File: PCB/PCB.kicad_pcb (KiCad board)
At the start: 2 copper layers, 16 parts, among them J1 USB_B_Micro, Q1 PJA3428, Q2 PJA3428, Q3 AO3401A, Q4 BD441, U2 CP2102N-Axx-xQFN24, U4 LM2578

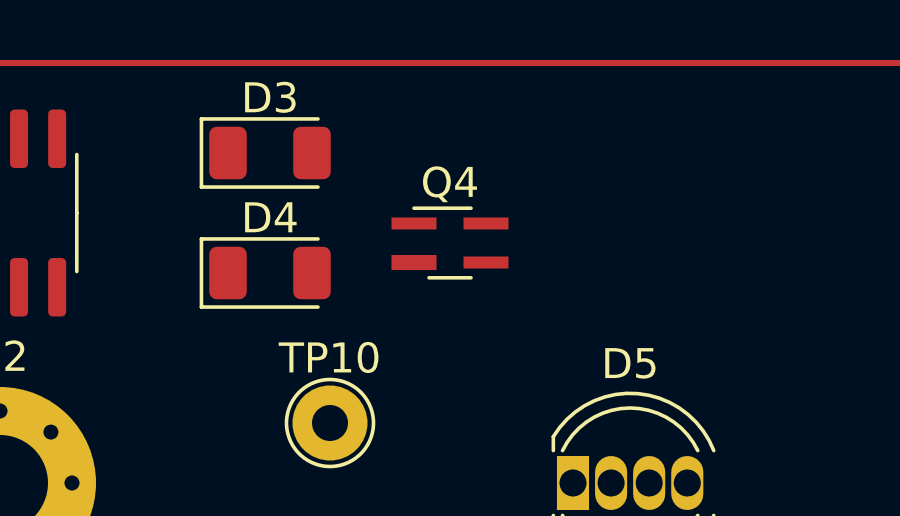
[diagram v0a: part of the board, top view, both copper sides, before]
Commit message: pcb update (transistors)
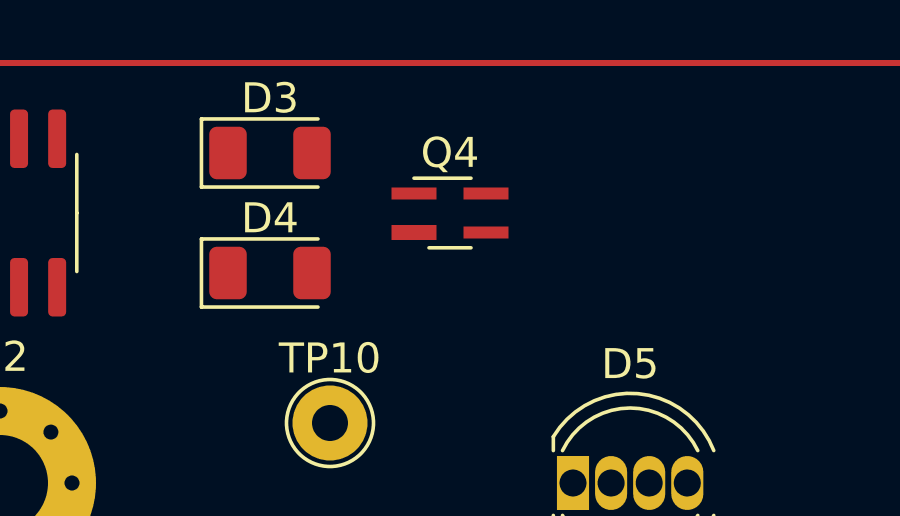
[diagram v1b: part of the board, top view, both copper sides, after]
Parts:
- Q4: value BD441 -> BC546
- moved Q4 1.00 mm to (149.0, 96.0)
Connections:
- Q4 pad 1: GND -> Net-(D4-Pad2)
- Q4 pad 2: Net-(D4-Pad2) -> Net-(R14-Pad1)
- Q4 pad 3: Net-(Q4-Pad3) -> GND

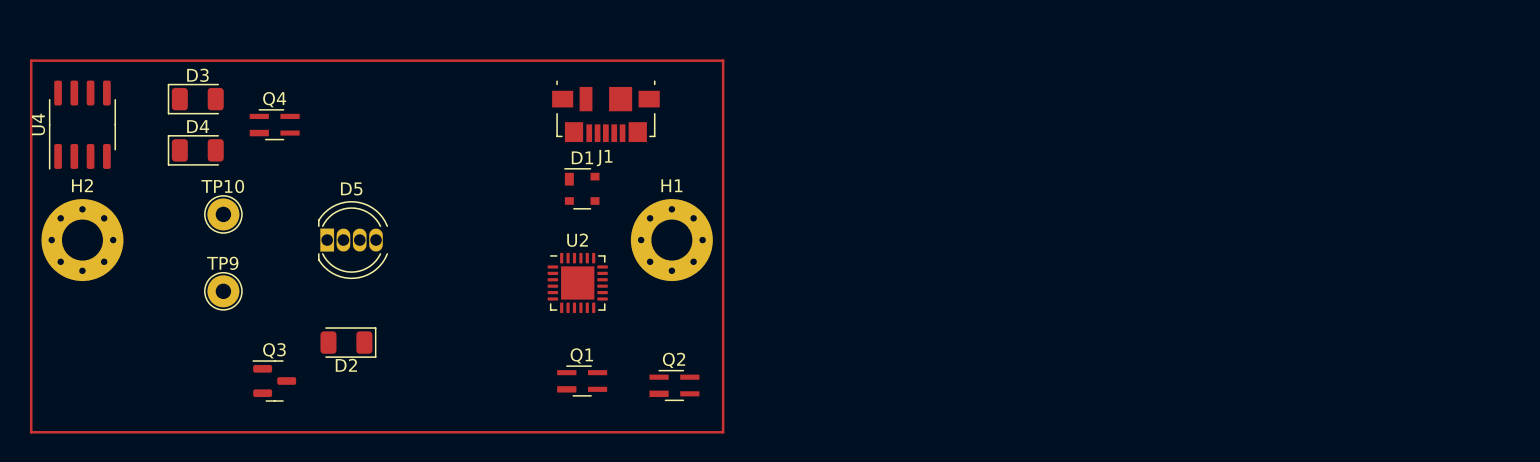
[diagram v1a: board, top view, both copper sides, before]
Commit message: edge cut improvement and general placements for mechanical design
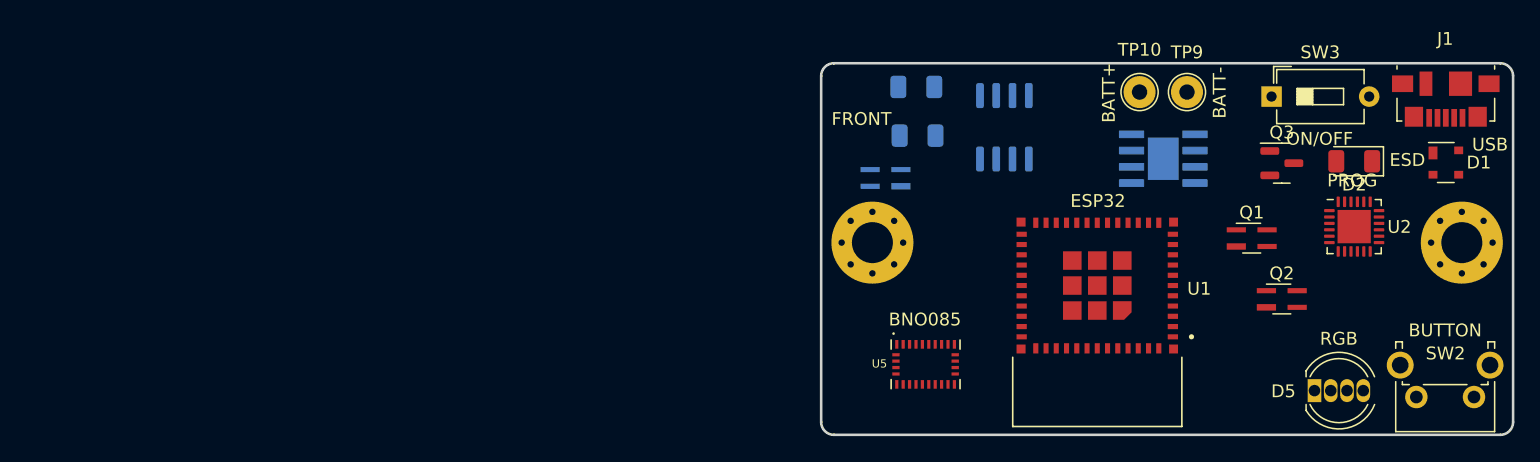
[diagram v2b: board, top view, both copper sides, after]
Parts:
- added SW2: SW_Push, Button_Switch_THT:SW_Tactile_SPST_Angled_PTS645Vx58-2LFS, F.Cu at (242.6, 117.2)
- added SW3: ON/OFF, Button_Switch_THT:SW_DIP_SPSTx01_Slide_6.7x4.1mm_W7.62mm_P2.54mm_LowProfile, F.Cu at (226.8, 93.8)
- added U1: ESP32-PICO-MINI-02, ESP32-PICO-MINI-02:MODULE_ESP32-PICO-MINI-02, F.Cu at (213.2, 108.5)
- added U3: TP4056, TP4056:SOP127P600X175-9N, B.Cu at (218.3, 98.7)
- added U5: BNO080, BNO080:IC_BNO080, F.Cu at (199.8, 114.7)
- D3, D4, Q4, U4: moved to B.Cu
- moved Q3 80.4 mm to (227.6, 99.0)
- moved D2 79.9 mm to (233.2, 98.8)
- moved D5 77.9 mm to (230.2, 116.8)
- moved TP9 76.8 mm to (220.2, 93.5)
- moved TP10 72.1 mm to (216.5, 93.5)
- moved U4 72.0 mm to (205.9, 96.2)
- moved D1 67.4 mm to (240.4, 99.0)
- moved J1 65.6 mm to (240.4, 94.0)
- moved H1 61.7 mm to (241.7, 105.2)
- moved H2 61.7 mm to (195.7, 105.2)
- moved U2 60.8 mm to (233.2, 104.0)
- moved D4 56.2 mm to (199.2, 96.8), turned to 180 degrees
- moved D3 56.1 mm to (199.1, 93.0), turned to 180 degrees
- moved Q1 53.4 mm to (225.2, 104.8)
- moved Q2 47.9 mm to (227.6, 109.6)
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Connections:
- U2 pad 18: FTDI_CTS -> (no net)
- U2 pad 19: FTDI_RTS -> (no net)
- U2 pad 20: FTDI_RX -> (no net)
- U2 pad 21: FTDI_TX -> (no net)
- U2 pad 23: FTDI_DTR -> (no net)
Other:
- board outline added: 54 x 29 mm
- board text added: "BACK"
- board text added: "BATT+"
- board text added: "BATT-"
- board text added: "BNO085"
- board text added: "BUTTON"
- board text added: "ESD"
- board text added: "ESP32"
- board text added: "FRONT"
- board text added: "LM2578"
- board text added: "ON/OFF"
- board text added: "PROG"
- board text added: "RGB"
- board text added: "TP4056"
- board text added: "USB"

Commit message: huuuuge progress
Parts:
- added C1: 10uF, Capacitor_SMD:C_0603_1608Metric, F.Cu at (240.9, 66.1)
- added C10: 100nF, Capacitor_SMD:C_0603_1608Metric, F.Cu at (236.3, 103.9)
- added C11: 100nF, Capacitor_SMD:C_0603_1608Metric, F.Cu at (198.7, 118.4)
- added C15: 22pf, Capacitor_SMD:C_0603_1608Metric, F.Cu at (201.5, 109.4)
- added C16: 22pf, Capacitor_SMD:C_0603_1608Metric, F.Cu at (194.2, 109.4)
- added C18: 12pf, Capacitor_SMD:C_0603_1608Metric, F.Cu at (269.6, 43.3)
- added C19: 12pf, Capacitor_SMD:C_0603_1608Metric, F.Cu at (255.7, 57.8)
- added C2: 1uF, Capacitor_SMD:C_0603_1608Metric, F.Cu at (251.2, 61.4)
- added C20: 1uF, Capacitor_SMD:C_0603_1608Metric, F.Cu at (251.7, 57.8)
- added C21: 10uF, Capacitor_SMD:C_1206_3216Metric, B.Cu at (236.9, 98.5)
- added C22: 10uF, Capacitor_SMD:C_1206_3216Metric, B.Cu at (231.9, 92.6)
- added C23: 100nF, Capacitor_SMD:C_0603_1608Metric, F.Cu at (193.4, 113.4)
- added C24: 100nF, Capacitor_SMD:C_0603_1608Metric, F.Cu at (193.4, 111.8)
- added C3: 10uF, Capacitor_SMD:C_0603_1608Metric, F.Cu at (265.6, 45.8)
- added C4: 1uF, Capacitor_SMD:C_0603_1608Metric, F.Cu at (248.9, 64.0)
- added C5: 100nF, Capacitor_SMD:C_0603_1608Metric, F.Cu at (237.8, 72.5)
- added C6: 100nF, Capacitor_SMD:C_0603_1608Metric, F.Cu at (256.9, 50.9)
- added C7: 10uF, Capacitor_SMD:C_1206_3216Metric, F.Cu at (224.5, 96.2)
- added C8: 100nF, Capacitor_SMD:C_0603_1608Metric, F.Cu at (233.3, 102.2)
- added C9: 1uF, Capacitor_SMD:C_0603_1608Metric, F.Cu at (237.9, 103.9)
- added D6: LED_RGB, LED_THT:LED_D5.0mm-4_RGB, F.Cu at (234.6, 116.8)
- added D7: Red, LED_SMD:LED_0805_2012Metric_Pad1.15x1.40mm_HandSolder, B.Cu at (231.6, 95.0)
- added D8: Green, LED_SMD:LED_0805_2012Metric_Pad1.15x1.40mm_HandSolder, B.Cu at (231.6, 97.1)
- added F1: 500mA, 0ZCJ0050FF2G:RESC3216X125N, F.Cu at (229.3, 97.2)
- added R1: 10k, Resistor_SMD:R_0603_1608Metric, F.Cu at (232.3, 76.0)
- added R11: 10k, Resistor_SMD:R_0603_1608Metric, F.Cu at (200.3, 118.4)
- added R15: 3.3k, Resistor_SMD:R_0603_1608Metric, F.Cu at (204.7, 106.9)
- added R16: 3.3k, Resistor_SMD:R_0603_1608Metric, F.Cu at (203.1, 106.9)
- added R17: 1k, Resistor_SMD:R_0603_1608Metric, F.Cu at (244.9, 64.0)
- added R18: 10k, Resistor_SMD:R_0603_1608Metric, F.Cu at (251.7, 55.3)
- added R19: 470, Resistor_SMD:R_0603_1608Metric, F.Cu at (225.3, 94.2)
- added R2: 10k, Resistor_SMD:R_0603_1608Metric, F.Cu at (248.9, 66.5)
- added R20: 2k, Resistor_SMD:R_0603_1608Metric, B.Cu at (243.9, 93.7)
- added R21: 10k, Resistor_SMD:R_0603_1608Metric, F.Cu at (241.8, 69.0)
- added R22: 470, Resistor_SMD:R_0603_1608Metric, B.Cu at (227.9, 95.2)
- added R23: 470, Resistor_SMD:R_0603_1608Metric, B.Cu at (227.9, 96.9)
- added R24: 3.3k, Resistor_SMD:R_0603_1608Metric, F.Cu at (265.4, 48.3)
- added R25: 3.3k, Resistor_SMD:R_0603_1608Metric, F.Cu at (236.3, 75.0)
- added R3: 10k, Resistor_SMD:R_0603_1608Metric, F.Cu at (228.3, 76.0)
- added R4: 10k, Resistor_SMD:R_0603_1608Metric, F.Cu at (244.9, 66.5)
- added R5: 22k, Resistor_SMD:R_0603_1608Metric, F.Cu at (237.9, 100.8)
- added R6: 47k, Resistor_SMD:R_0603_1608Metric, F.Cu at (236.3, 100.8)
- added R7: 10k, Resistor_SMD:R_0603_1608Metric, F.Cu at (204.1, 113.7)
- added R8: 10k, Resistor_SMD:R_0603_1608Metric, F.Cu at (193.4, 115.0)
- added SW1: SW_Push, Button_Switch_SMD:SW_SPST_CK_KXT3, F.Cu at (218.4, 67.9)
- added SW4: ON/OFF, footprints:CUS-12TB, F.Cu at (231.4, 92.7)
- added TP11: ~{RESET}_TP, TestPoint:TestPoint_Pad_D1.0mm, F.Cu at (243.8, 74.8)
- added TP12: GPIO0_TP, TestPoint:TestPoint_Pad_D1.0mm, F.Cu at (252.4, 67.3)
- added TP13: SDA_TP, TestPoint:TestPoint_Pad_D1.0mm, F.Cu at (259.2, 59.1)
- added TP14: SCL_TP, TestPoint:TestPoint_Pad_D1.0mm, F.Cu at (249.4, 69.2)
- added TP15: INT_TP, TestPoint:TestPoint_Pad_D1.0mm, F.Cu at (202.3, 117.8)
- added TP3: InputVoltage_TP, TestPoint:TestPoint_Pad_D1.0mm, F.Cu at (268.9, 48.6)
- added TP4: TX_TP, TestPoint:TestPoint_Pad_D1.0mm, F.Cu at (273.1, 46.6)
- added TP5: RX_TP, TestPoint:TestPoint_Pad_D1.0mm, F.Cu at (252.4, 64.2)
- added TP6: RTS_TP, TestPoint:TestPoint_Pad_D1.0mm, F.Cu at (259.2, 56.1)
- added TP7: CTS_TP, TestPoint:TestPoint_Pad_D1.0mm, F.Cu at (245.4, 71.8)
- added TP8: DTR_TP, TestPoint:TestPoint_Pad_D1.0mm, F.Cu at (262.3, 56.1)
- added Y1: 32.768 kHz, Crystal:Crystal_SMD_EuroQuartz_EQ161-2Pin_3.2x1.5mm, F.Cu at (197.9, 109.8)
- added Y2: 32.768 kHz, Crystal:Crystal_SMD_EuroQuartz_EQ161-2Pin_3.2x1.5mm, F.Cu at (235.8, 67.0)
- D5: value LED_RGBA -> PowerLed; footprint LED_THT:LED_D5.0mm-4_RGB -> LED_SMD:LED_0805_2012Metric_Pad1.15x1.40mm_HandSolder
- H1, H2: footprint MountingHole:MountingHole_3.2mm_M3_Pad_Via -> MountingHole:MountingHole_2.2mm_M2_Pad_Via
- SW2: footprint Button_Switch_THT:SW_Tactile_SPST_Angled_PTS645Vx58-2LFS -> Button_Switch_SMD:SW_SPST_CK_KXT3
- SW3: value ON/OFF -> SW_Push; footprint Button_Switch_THT:SW_DIP_SPSTx01_Slide_6.7x4.1mm_W7.62mm_P2.54mm_LowProfile -> Button_Switch_SMD:SW_SPST_CK_KXT3
- U1: footprint ESP32-PICO-MINI-02:MODULE_ESP32-PICO-MINI-02 -> ESP32:MODULE_ESP32-PICO-MINI-02
- U4: moved to F.Cu
- moved SW2 59.6 mm to (218.4, 62.7), turned to 0 degrees
- moved SW3 49.7 mm to (233.9, 44.6)
- moved U4 25.2 mm to (217.2, 73.7), turned to 0 degrees
- moved D5 24.9 mm to (224.9, 92.4), turned to 180 degrees
- moved U3 20.5 mm to (238.3, 94.3)
- moved TP10 15.1 mm to (230.0, 100.2)
- moved TP9 9.20 mm to (226.4, 100.2)
- moved Q3 6.08 mm to (233.6, 98.0), turned to -90 degrees
- moved D2 4.73 mm to (237.9, 98.0), turned to 0 degrees
- moved Q2 4.32 mm to (223.4, 110.6), turned to 180 degrees
- moved Q1 3.29 mm to (223.3, 107.5)
- moved D1 3.26 mm to (243.7, 98.7), turned to -90 degrees
- moved U2 2.74 mm to (232.1, 106.5), turned to 180 degrees
- moved H1 1.25 mm to (242.8, 105.7)
- moved H2 1.25 mm to (194.5, 105.7)
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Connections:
- D1 pad 2: USB_D+ -> USB_D-
- D1 pad 3: USB_D- -> USB_D+
- D5 pad 1: unconnected-(D5-Pad1) -> GND
- D5 pad 2: unconnected-(D5-Pad2) -> Net-(D5-Pad2)
- SW2 pad 1: (no net) -> Net-(R17-Pad1)
- SW2 pad 2: (no net) -> +3V3
- SW3 pad 1: (no net) -> GND
- SW3 pad 2: (no net) -> SESSION_BUTTON
- TP10 pad 1: unconnected-(TP10-Pad1) -> +BATT
- TP9 pad 1: unconnected-(TP9-Pad1) -> GND
- U1 pad 10: (no net) -> unconnected-(U1-Pad10)
- U1 pad 12: (no net) -> XTAL_0
- U1 pad 13: (no net) -> XTAL_1
- U1 pad 15: (no net) -> unconnected-(U1-Pad15)
- U1 pad 16: (no net) -> unconnected-(U1-Pad16)
- U1 pad 17: (no net) -> ~{BNO_RST}
- U1 pad 18: (no net) -> RGB_BLUE
- U1 pad 19: (no net) -> RGB_RED
- U1 pad 20: (no net) -> RGB_GREEN
- U1 pad 21: (no net) -> unconnected-(U1-Pad21)
- U1 pad 22: (no net) -> Net-(R3-Pad2)
- U1 pad 24: (no net) -> BNO_INTERRUPT
- U1 pad 25: (no net) -> unconnected-(U1-Pad25)
- U1 pad 26: (no net) -> I2C_SCL
- U1 pad 27: (no net) -> unconnected-(U1-Pad27)
- U1 pad 28: (no net) -> unconnected-(U1-Pad28)
- U1 pad 29: (no net) -> unconnected-(U1-Pad29)
- U1 pad 30: (no net) -> FTDI_TX
- U1 pad 31: (no net) -> FTDI_RX
- U1 pad 32: (no net) -> unconnected-(U1-Pad32)
- U1 pad 33: (no net) -> unconnected-(U1-Pad33)
- U1 pad 34: (no net) -> I2C_SDA
- U1 pad 35: (no net) -> unconnected-(U1-Pad35)
- U1 pad 4: (no net) -> unconnected-(U1-Pad4)
- U1 pad 5: (no net) -> unconnected-(U1-Pad5)
- U1 pad 6: (no net) -> unconnected-(U1-Pad6)
- U1 pad 7: (no net) -> unconnected-(U1-Pad7)
- U1 pad 9: (no net) -> BATT_READ
- U2 pad 18: (no net) -> FTDI_CTS
- U2 pad 19: (no net) -> FTDI_RTS
- U2 pad 20: (no net) -> FTDI_RX
- U2 pad 21: (no net) -> FTDI_TX
- U2 pad 23: (no net) -> FTDI_DTR
- U2 pad 9: ~{RESET} -> +3V3
- U3 pad 1: (no net) -> GND
- U3 pad 2: (no net) -> Net-(R20-Pad2)
- U3 pad 3: (no net) -> GND
- U3 pad 4: (no net) -> +5V
- U3 pad 5: (no net) -> +BATT
- U3 pad 6: (no net) -> ~{STDBY}
- U3 pad 7: (no net) -> ~{CHRG}
- U3 pad 8: (no net) -> +5V
- U3 pad 9: (no net) -> unconnected-(U3-Pad9)
- U5 pad 11: (no net) -> ~{BNO_RST}
- U5 pad 14: (no net) -> BNO_INTERRUPT
- U5 pad 15: (no net) -> Net-(R15-Pad2)
- U5 pad 16: (no net) -> Net-(R16-Pad2)
- U5 pad 18: (no net) -> Net-(R7-Pad2)
- U5 pad 19: (no net) -> I2C_SCL
- U5 pad 20: (no net) -> I2C_SDA
- U5 pad 26: (no net) -> Net-(C15-Pad1)
- U5 pad 27: (no net) -> Net-(C16-Pad1)
- U5 pad 28: (no net) -> +3.3V
- U5 pad 3: (no net) -> +3.3V
- U5 pad 4: (no net) -> Net-(R8-Pad2)
- U5 pad 9: (no net) -> Net-(C11-Pad1)
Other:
- board text removed: "BACK"
- board text removed: "BATT+"
- board text removed: "BATT-"
- board text removed: "BNO085"
- board text removed: "BUTTON"
- board text removed: "ESD"
- board text removed: "ESP32"
- board text removed: "FRONT"
- board text removed: "LM2578"
- board text removed: "ON/OFF"
- board text removed: "PROG"
- board text removed: "RGB"
- board text removed: "TP4056"
- board text removed: "USB"

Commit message: bno
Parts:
- D3, D4, Q4: moved to F.Cu
- TP15, TP7: moved to B.Cu
- moved R24 87.3 mm to (204.9, 111.3), turned to -90 degrees
- moved C3 82.2 mm to (221.6, 115.2), turned to 90 degrees
- moved TP13 78.4 mm to (204.9, 115.7)
- moved C18 76.7 mm to (216.3, 98.5), turned to 90 degrees
- moved TP4 75.7 mm to (234.5, 111.7)
- moved SW3 73.3 mm to (242.4, 117.4)
- moved C6 70.0 mm to (223.1, 112.1), turned to -90 degrees
- moved TP3 65.3 mm to (222.7, 94.8)
- moved TP6 62.6 mm to (230.2, 111.5)
- moved TP8 61.3 mm to (236.6, 111.7)
- moved TP14 59.0 mm to (203.0, 105.7)
- moved C19 54.9 mm to (218.9, 98.5), turned to 90 degrees
- moved C4 53.9 mm to (224.7, 112.1), turned to -90 degrees
- moved C1 52.2 mm to (223.1, 115.2), turned to 90 degrees
- moved TP5 51.4 mm to (232.4, 111.5)
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
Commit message: more placements
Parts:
- added R26: 20k, Resistor_SMD:R_0603_1608Metric, F.Cu at (251.6, 92.9)
- added R27: 27k, Resistor_SMD:R_0603_1608Metric, F.Cu at (255.6, 92.9)
- SW3: footprint Button_Switch_SMD:SW_SPST_CK_KXT3 -> Button_Switch_THT:SW_Tactile_SPST_Angled_PTS645Vx58-2LFS
- moved D6 5.49 mm to (229.2, 116.2)
- moved R21 3.17 mm to (244.3, 111.3)
- moved SW3 0.18 mm to (242.6, 117.4), turned to 180 degrees
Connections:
- SW3 pad 1: GND -> SESSION_BUTTON
- SW3 pad 2: SESSION_BUTTON -> GND
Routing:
- added copper zone on In1.Cu, net +3.3V
- added copper zone on In2.Cu, net GND
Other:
- copper layers 2 -> 4

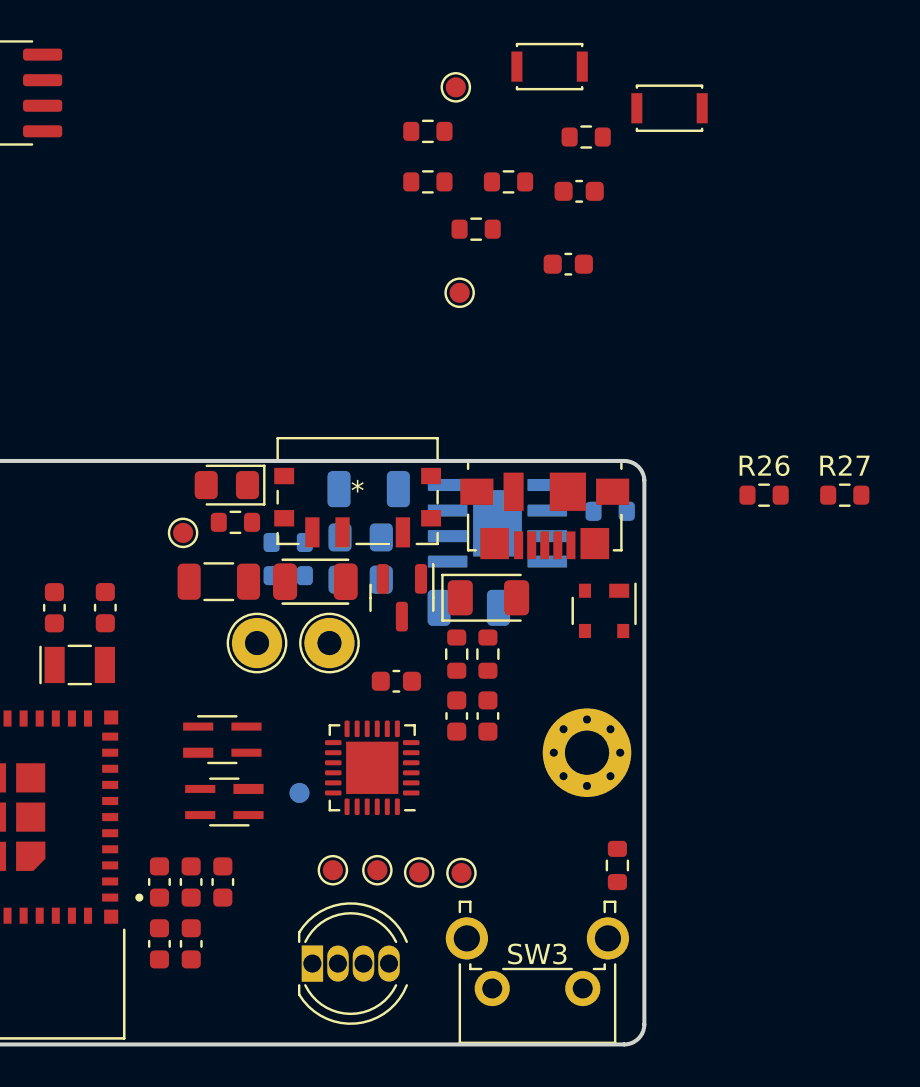
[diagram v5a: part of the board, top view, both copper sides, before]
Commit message: placements for everything besides buck/boost
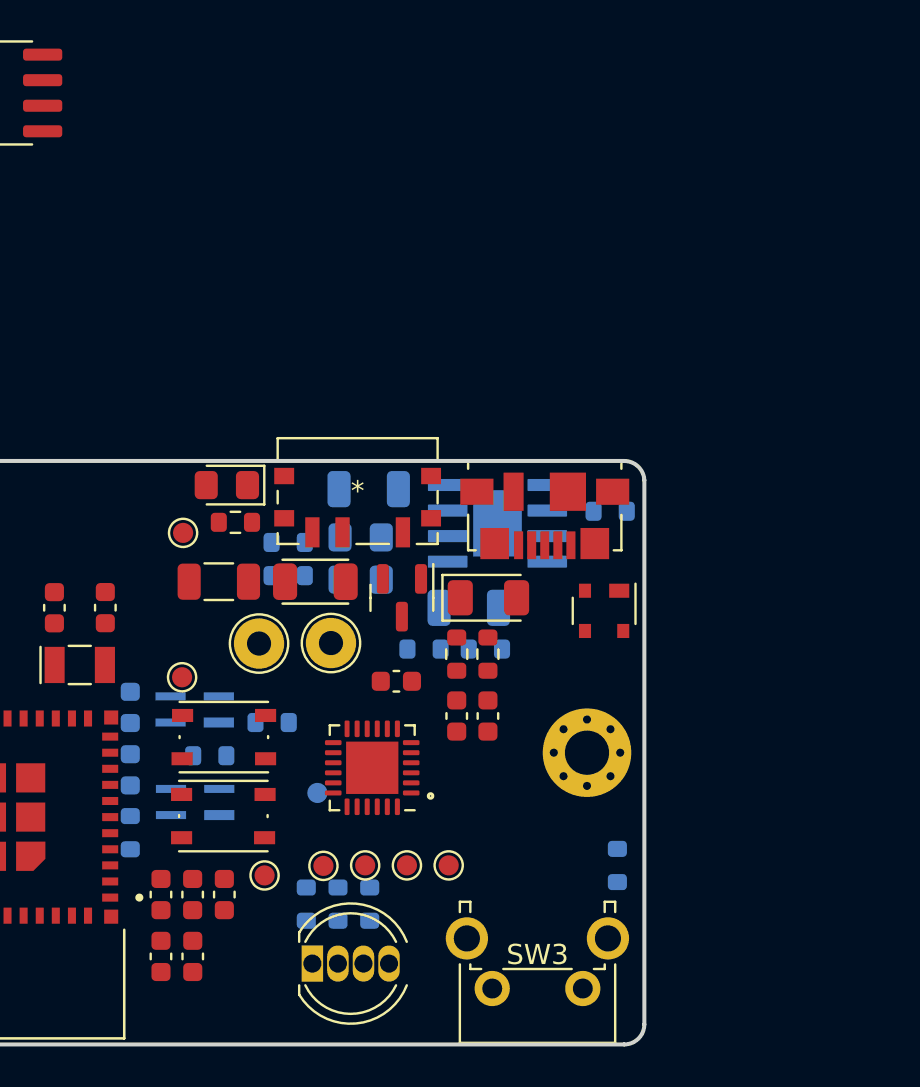
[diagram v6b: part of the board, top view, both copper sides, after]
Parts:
- added R28: 470, Resistor_SMD:R_0603_1608Metric, B.Cu at (232.0, 113.2)
- C2, Q1, Q2, R1, R2, R21, R26, R27, R4: moved to B.Cu
- C20: value 1uF -> 100nF; moved to B.Cu
- R17: value 1k -> 470; moved to B.Cu
- R18: value 10k -> 470; moved to B.Cu
- SW1, SW2: footprint Button_Switch_SMD:SW_SPST_CK_KXT3 -> Button_Switch_SMD:SW_Push_1P1T_NO_Vertical_Wuerth_434133025816
- moved SW1 41.6 mm to (224.7, 108.8)
- moved R18 40.1 mm to (230.4, 113.2), turned to -90 degrees
- moved R17 38.9 mm to (228.8, 113.2), turned to 90 degrees
- moved SW2 37.0 mm to (224.8, 104.9), turned to 180 degrees
- moved R4 35.6 mm to (220.1, 109.7), turned to 90 degrees
- moved C20 34.0 mm to (220.1, 103.5), turned to 90 degrees
- moved C2 33.2 mm to (220.1, 106.5), turned to 90 degrees
- moved TP12 32.3 mm to (222.7, 102.0)
- moved TP11 30.5 mm to (226.8, 111.8)
- moved R1 29.3 mm to (224.1, 105.8)
- moved R2 29.3 mm to (227.2, 104.2), turned to 180 degrees
- moved R27 19.4 mm to (237.8, 100.5)
- moved R26 18.6 mm to (234.7, 100.5)
- moved Q1 2.03 mm to (223.3, 103.5), turned to 180 degrees
- moved Q2 1.45 mm to (223.3, 108.2)
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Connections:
- net FTDI_CTS renamed PROG_CTS
- net FTDI_DTR renamed PROG_DTR
- net FTDI_RTS renamed PROG_RTS
- net FTDI_RX renamed PROG_RX
- net FTDI_TX renamed PROG_TX
- C20 pad 1: GND -> GPIO0
- C20 pad 2: GPIO0 -> GND
- D6 pad 1: RGB_RED -> Net-(D6-Pad1)
- D6 pad 2: RGB_GREEN -> Net-(D6-Pad2)
- D6 pad 3: RGB_BLUE -> Net-(D6-Pad3)
- D7 pad 1: Net-(D7-Pad1) -> ~{CHRG}
- D7 pad 2: ~{CHRG} -> Net-(R22-Pad2)
- D8 pad 1: Net-(D8-Pad1) -> ~{STDBY}
- D8 pad 2: ~{STDBY} -> Net-(R23-Pad2)
- R17 pad 1: Net-(R17-Pad1) -> Net-(D6-Pad1)
- R17 pad 2: GPIO0 -> RGB_RED
- R18 pad 1: GPIO0 -> Net-(D6-Pad2)
- R18 pad 2: GND -> RGB_GREEN
- R22 pad 1: GND -> +3V3
- R22 pad 2: Net-(D7-Pad1) -> Net-(R22-Pad2)
- R23 pad 1: GND -> +3V3
- R23 pad 2: Net-(D8-Pad1) -> Net-(R23-Pad2)
- R26 pad 1: +3V3 -> +BATT
- SW2 pad 1: Net-(R17-Pad1) -> GND
- SW2 pad 2: +3V3 -> GPIO0
- U1 pad 10: unconnected-(U1-Pad10) -> BATT_READ
- U1 pad 15: unconnected-(U1-Pad15) -> RGB_RED
- U1 pad 16: unconnected-(U1-Pad16) -> RGB_GREEN
- U1 pad 17: ~{BNO_RST} -> RGB_BLUE
- U1 pad 18: RGB_BLUE -> unconnected-(U1-Pad18)
- U1 pad 19: RGB_RED -> unconnected-(U1-Pad19)
- U1 pad 20: RGB_GREEN -> ~{BNO_RST}
- U1 pad 24: BNO_INTERRUPT -> unconnected-(U1-Pad24)
- U1 pad 33: unconnected-(U1-Pad33) -> BNO_INTERRUPT
- U1 pad 9: BATT_READ -> unconnected-(U1-Pad9)

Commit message: starting routing
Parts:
- moved C21 0.68 mm to (236.9, 99.2)
- moved R27 0.68 mm to (237.7, 101.2)
- moved U3 0.68 mm to (238.3, 95.0)
- moved R26 0.68 mm to (234.7, 101.2)
- moved R20 0.65 mm to (243.3, 93.7), turned to -90 degrees
- turned D7 to 180 degrees
- turned D8 to 180 degrees
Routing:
- net +5V: track 0.00 -> 39.4 mm, vias 0 -> 2
- net USB_D+: track 0.00 -> 18.7 mm
- net USB_D-: track 0.00 -> 18.5 mm, vias 0 -> 2
- net +BATT: track 0.00 -> 11.2 mm, vias 0 -> 1
- net GND: track 0.00 -> 10.6 mm, vias 0 -> 1
- net Net-(D2-Pad1): track 0.00 -> 7.36 mm
- net +3V3: track 0.00 -> 7.25 mm, vias 0 -> 1
- net Vin: track 0.00 -> 4.84 mm
- net ~{STDBY}: track 0.00 -> 3.89 mm
- net ~{CHRG}: track 0.00 -> 3.55 mm
- net Net-(R20-Pad2): track 0.00 -> 2.56 mm
- net Net-(F1-Pad1): track 0.00 -> 2.52 mm
- net Net-(R22-Pad2): track 0.00 -> 1.85 mm
- net Net-(R23-Pad2): track 0.00 -> 1.83 mm
- net Net-(R5-Pad2): track 0.00 -> 1.55 mm
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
